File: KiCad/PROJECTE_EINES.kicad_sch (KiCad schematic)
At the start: 5 parts

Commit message: Errors solucionats
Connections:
- net VBAT_12V renamed +12V
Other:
- sheet ETAPA DE ALIMENTACIO ports: added none; removed VBAT_12V, VDD_3V3
- sheet MICROCONTROLADOR I DEBUG ports: added none; removed VDD_3V3
- sheet SENSORS ports: added none; removed VDD_3V3
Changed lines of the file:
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@@
+	(wire
+		(pts
+			(xy 27.94 44.45) (xy 34.29 44.45)
+		)
+		(stroke
+			(width 0)
+			(type default)
+		)
+	)
 	(wire
 		(pts
@@
 	(wire
 		(pts
-			(xy 172.72 58.42) (xy 171.45 58.42)
+			(xy 22.86 93.98) (xy 27.94 93.98)
 		)
 		(stroke
@@
 		)
 	)
-	(wire
-		(pts
-			(xy 22.86 93.98) (xy 27.94 93.98)
-		)
-		(stroke
-			(width 0)
-			(type default)
-		)
-	)
 	(global_label "WIN_MOTOR_B"
 		(shape output)
@@
 		)
 	)
-	(global_label "VDD_3V3"
-		(shape input)
-		(at 194.31 36.83 180)
-		(effects
-			(font
-				(size 1.27 1.27)
-			)
-			(justify right)
-		)
-		(property "Intersheetrefs" "${INTERSHEET_REFS}"
-			(at 194.31 36.83 0)
-			(effects
-				(font
-					(size 1.27 1.27)
-				)
-				(hide yes)
-			)
-		)
-	)
 	(global_label "DOOR_INA"
 		(shape output)
@@
 		)
 	)
-	(global_label "VBAT_12V"
-		(shape input)
-		(at 27.94 44.45 0)
-		(effects
-			(font
-				(size 1.27 1.27)
-			)
-			(justify left)
-		)
-		(property "Intersheetrefs" "${INTERSHEET_REFS}"
-			(at 27.94 44.45 0)
-			(effects
-				(font
-					(size 1.27 1.27)
-				)
-				(hide yes)
-			)
-		)
-	)
 	(global_label "UART_RX"
 		(shape output)
@@
 		)
 	)
-	(global_label "VDD_3V3"
-		(shape input)
-		(at 40.64 24.13 0)
-		(effects
-			(font
-				(size 1.27 1.27)
-			)
-			(justify left)
-		)
-		(property "Intersheetrefs" "${INTERSHEET_REFS}"
-			(at 40.64 24.13 90)
-			(effects
-				(font
-					(size 1.27 1.27)
-				)
-				(hide yes)
-			)
-		)
-	)
 	(global_label "DOOR_MOTOR_B"
 		(shape output)
@@
 		)
 	)
-	(global_label "VDD_3V3"
-		(shape output)
-		(at 104.14 67.31 0)
-		(effects
-			(font
-				(size 1.27 1.27)
-			)
-			(justify left)
-		)
-		(property "Intersheetrefs" "${INTERSHEET_REFS}"
-			(at 104.14 67.31 0)
-			(effects
-				(font
-					(size 1.27 1.27)
-				)
-				(hide yes)
-			)
-		)
-	)
 	(global_label "WIN_DIAGA"
 		(shape output)
@@
 		)
 	)
-	(global_label "VDD_3V3"
-		(shape input)
-		(at 118.11 83.82 90)
-		(effects
-			(font
-				(size 1.27 1.27)
-			)
-			(justify left)
-		)
-		(property "Intersheetrefs" "${INTERSHEET_REFS}"
-			(at 118.11 83.82 0)
-			(effects
-				(font
-					(size 1.27 1.27)
-				)
-				(hide yes)
-			)
-		)
-	)
 	(global_label "DOOR_PWM"
 		(shape output)
@@
 		)
 	)
-	(global_label "VBAT_12V"
-		(shape input)
-		(at 60.96 49.53 180)
-		(effects
-			(font
-				(size 1.27 1.27)
-			)
-			(justify right)
-		)
-		(property "Intersheetrefs" "${INTERSHEET_REFS}"
-			(at 60.96 49.53 0)
-			(effects
-				(font
-					(size 1.27 1.27)
-				)
-				(hide yes)
+	(symbol
+		(lib_id "power:+3.3V")
+		(at 40.64 24.13 0)
+		(unit 1)
+		(exclude_from_sim no)
+		(in_bom yes)
+		(on_board yes)
+		(dnp no)
+		(fields_autoplaced yes)
+		(property "Reference" "#PWR03"
+			(at 40.64 27.94 0)
+			(effects
+				(font
+					(size 1.27 1.27)
+				)
+				(hide yes)
+			)
+		)
+		(property "Value" "+3.3V"
+			(at 40.64 19.05 0)
+			(effects
+				(font
+					(size 1.27 1.27)
+				)
+			)
+		)
+		(property "Footprint" ""
+			(at 40.64 24.13 0)
+			(effects
+				(font
+					(size 1.27 1.27)
+				)
+				(hide yes)
+			)
+		)
+		(property "Datasheet" ""
+			(at 40.64 24.13 0)
+			(effects
+				(font
+					(size 1.27 1.27)
+				)
+				(hide yes)
+			)
+		)
+		(property "Description" "Power symbol creates a global label with name \"+3.3V\""
+			(at 40.64 24.13 0)
+			(effects
+				(font
+					(size 1.27 1.27)
+				)
+				(hide yes)
+			)
+		)
+		(pin "1"
+		)
+		(instances
+			(project ""
+				(path "/347831db-5db9-4aff-ad32-e56fd770e219"
+					(reference "#PWR03")
+					(unit 1)
+				)
 			)
 		)
@@
 	)
 	(symbol
-		(lib_id "power:+3.3V")
-		(at 40.64 24.13 0)
-		(unit 1)
-		(exclude_from_sim no)
-		(in_bom yes)
-		(on_board yes)
-		(dnp no)
-		(fields_autoplaced yes)
-		(property "Reference" "#PWR03"
-			(at 40.64 27.94 0)
-			(effects
-				(font
-					(size 1.27 1.27)
-				)
-				(hide yes)
-			)
-		)
-		(property "Value" "+3.3V"
-			(at 40.64 19.05 0)
-			(effects
-				(font
-					(size 1.27 1.27)
-				)
-			)
-		)
-		(property "Footprint" ""
-			(at 40.64 24.13 0)
-			(effects
-				(font
-					(size 1.27 1.27)
-				)
-				(hide yes)
-			)
-		)
-		(property "Datasheet" ""
-			(at 40.64 24.13 0)
-			(effects
-				(font
-					(size 1.27 1.27)
-				)
-				(hide yes)
-			)
-		)
-		(property "Description" "Power symbol creates a global label with name \"+3.3V\""
-			(at 40.64 24.13 0)
-			(effects
-				(font
-					(size 1.27 1.27)
-				)
-				(hide yes)
-			)
-		)
-		(pin "1"
-		)
-		(instances
-			(project ""
-				(path "/347831db-5db9-4aff-ad32-e56fd770e219"
-					(reference "#PWR03")
-					(unit 1)
-				)
-			)
-		)
-	)
-	(symbol
 		(lib_id "Connector:Conn_01x02_Pin")
 		(at 21.59 77.47 0)
@@
 				(path "/347831db-5db9-4aff-ad32-e56fd770e219"
 					(reference "J_MOTOR_DOOR1")
+					(unit 1)
+				)
+			)
+		)
+	)
+	(symbol
+		(lib_id "power:+12V")
+		(at 34.29 44.45 0)
+		(unit 1)
+		(exclude_from_sim no)
+		(in_bom yes)
+		(on_board yes)
+		(dnp no)
+		(fields_autoplaced yes)
+		(property "Reference" "#PWR051"
+			(at 34.29 48.26 0)
+			(effects
+				(font
+					(size 1.27 1.27)
+				)
+				(hide yes)
+			)
+		)
+		(property "Value" "+12V"
+			(at 34.29 39.37 0)
+			(effects
+				(font
+					(size 1.27 1.27)
+				)
+			)
+		)
+		(property "Footprint" ""
+			(at 34.29 44.45 0)
+			(effects
+				(font
+					(size 1.27 1.27)
+				)
+				(hide yes)
+			)
+		)
+		(property "Datasheet" ""
+			(at 34.29 44.45 0)
+			(effects
+				(font
+					(size 1.27 1.27)
+				)
+				(hide yes)
+			)
+		)
+		(property "Description" "Power symbol creates a global label with name \"+12V\""
+			(at 34.29 44.45 0)
+			(effects
+				(font
+					(size 1.27 1.27)
+				)
+				(hide yes)
+			)
+		)
+		(pin "1"
+		)
+		(instances
+			(project "PROJECTE_EINES"
+				(path "/347831db-5db9-4aff-ad32-e56fd770e219"
+					(reference "#PWR051")
 					(unit 1)
 				)
@@
 		(on_board yes)
 		(dnp no)
-		(property "Reference" "#FLG04"
+		(property "Reference" "#FLG01"
 			(at 22.86 92.075 0)
 			(effects
@@
 			(project "PROJECTE_EINES"
 				(path "/347831db-5db9-4aff-ad32-e56fd770e219"
-					(reference "#FLG04")
+					(reference "#FLG01")
 					(unit 1)
 				)
@@
 			)
 		)
-		(pin "VDD_3V3" input
-			(at 194.31 36.83 180)
-			(effects
-				(font
-					(size 1.27 1.27)
-				)
-				(justify left)
-			)
-		)
 		(pin "WIN_LIMIT" output
 			(at 194.31 44.45 180)
@@
 			)
 		)
-		(pin "VDD_3V3" input
-			(at 118.11 83.82 90)
-			(effects
-				(font
-					(size 1.27 1.27)
-				)
-				(justify right)
-			)
-		)
 		(pin "WIN_BTN_DOWN" input
 			(at 153.67 88.9 0)
@@
 			)
 		)
-		(pin "VBAT_12V" input
-			(at 60.96 49.53 180)
-			(effects
-				(font
-					(size 1.27 1.27)
-				)
-				(justify left)
-			)
-		)
 		(pin "VBAT_PROT" output
 			(at 104.14 64.77 0)
 			(effects
 				(font
-					(size 1.27 1.27)
-				)
-				(justify right)
-			)
-		)
-		(pin "VDD_3V3" output
-			(at 104.14 67.31 0)
-			(effects
-				(font

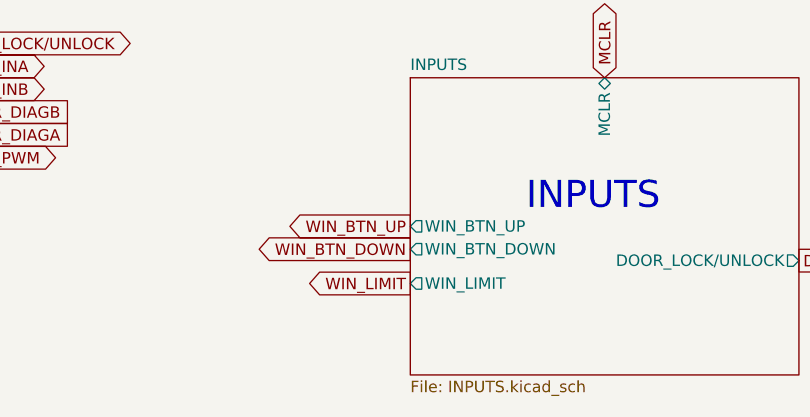
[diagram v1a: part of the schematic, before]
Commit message: REORDENACIÓ DEL MICRO
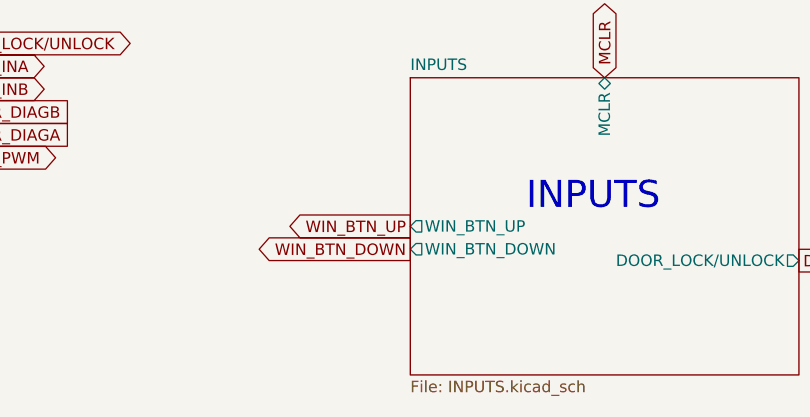
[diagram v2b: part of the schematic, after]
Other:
- sheet INPUTS ports: added none; removed WIN_LIMIT
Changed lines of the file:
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@@
-		)
-	)
-	(global_label "WIN_LIMIT"
-		(shape output)
-		(at 205.74 148.59 180)
-		(effects
-			(font
-				(size 1.27 1.27)
-			)
-			(justify right)
-		)
-		(property "Intersheetrefs" "${INTERSHEET_REFS}"
-			(at 205.74 148.59 0)
-			(effects
-				(font
-					(size 1.27 1.27)
-				)
-				(hide yes)
-			)
 		)
 	)
@@
 			(effects
 				(font
-					(size 1.27 1.27)
-				)
-				(justify left)
-			)
-		)
-		(pin "WIN_LIMIT" output
-			(at 205.74 148.59 180)
-			(effects
-				(font

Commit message: V1 Routing
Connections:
- net GND: now also J_DEBUG1.1 (Pin_1); no longer J_DEBUG1.3 (Pin_3)
- net MCLR: now also J_DEBUG1.3 (Pin_3); no longer J_DEBUG1.1 (Pin_1)
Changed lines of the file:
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@@
+	)
+	(junction
+		(at 30.48 21.59)
+		(diameter 0)
+		(color 0 0 0 0)
 	)
 	(junction
@@
 	(wire
 		(pts
-			(xy 26.67 24.13) (xy 40.64 24.13)
+			(xy 26.67 24.13) (xy 45.72 24.13)
 		)
 		(stroke
@@
 	(wire
 		(pts
-			(xy 40.64 26.67) (xy 40.64 27.94)
+			(xy 20.32 93.98) (xy 22.86 93.98)
 		)
 		(stroke
@@
 	(wire
 		(pts
-			(xy 20.32 93.98) (xy 22.86 93.98)
+			(xy 20.32 95.25) (xy 20.32 93.98)
 		)
 		(stroke
@@
 	(wire
 		(pts
-			(xy 20.32 95.25) (xy 20.32 93.98)
+			(xy 26.67 21.59) (xy 30.48 21.59)
 		)
 		(stroke
@@
 	(wire
 		(pts
-			(xy 26.67 26.67) (xy 40.64 26.67)
+			(xy 43.18 95.25) (xy 43.18 93.98)
 		)
 		(stroke
@@
 	(wire
 		(pts
-			(xy 43.18 95.25) (xy 43.18 93.98)
+			(xy 30.48 46.99) (xy 30.48 49.53)
 		)
 		(stroke
@@
 	(wire
 		(pts
-			(xy 30.48 46.99) (xy 30.48 49.53)
+			(xy 22.86 93.98) (xy 27.94 93.98)
 		)
 		(stroke
@@
 		)
 	)
-	(wire
-		(pts
-			(xy 22.86 93.98) (xy 27.94 93.98)
-		)
-		(stroke
-			(width 0)
-			(type default)
-		)
-	)
 	(global_label "WIN_MOTOR_B"
 		(shape output)
@@
 	(global_label "MCLR"
 		(shape input)
-		(at 26.67 21.59 0)
-		(effects
-			(font
-				(size 1.27 1.27)
-			)
-			(justify left)
-		)
-		(property "Intersheetrefs" "${INTERSHEET_REFS}"
-			(at 26.67 21.59 0)
+		(at 26.67 26.67 0)
+		(effects
+			(font
+				(size 1.27 1.27)
+			)
+			(justify left)
+		)
+		(property "Intersheetrefs" "${INTERSHEET_REFS}"
+			(at 26.67 26.67 0)
 			(effects
 				(font
@@
 	(symbol
 		(lib_id "power:+3.3V")
-		(at 40.64 24.13 0)
+		(at 45.72 24.13 0)
 		(unit 1)
 		(exclude_from_sim no)
@@
 		(dnp no)
 		(fields_autoplaced yes)
-		(property "Reference" "#PWR03"
-			(at 40.64 27.94 0)
+		(property "Reference" "#PWR04"
+			(at 45.72 27.94 0)
 			(effects
 				(font
@@
 		)
 		(property "Value" "+3.3V"
-			(at 40.64 19.05 0)
+			(at 45.72 19.05 0)
 			(effects
 				(font
@@
 		)
 		(property "Footprint" ""
-			(at 40.64 24.13 0)
+			(at 45.72 24.13 0)
 			(effects
 				(font
@@
 		)
 		(property "Datasheet" ""
-			(at 40.64 24.13 0)
+			(at 45.72 24.13 0)
 			(effects
 				(font
@@
 		)
 		(property "Description" "Power symbol creates a global label with name \"+3.3V\""
-			(at 40.64 24.13 0)
+			(at 45.72 24.13 0)
 			(effects
 				(font
@@
 			(project ""
 				(path "/347831db-5db9-4aff-ad32-e56fd770e219"
-					(reference "#PWR03")
+					(reference "#PWR04")
 					(unit 1)
 				)
@@
 		(dnp no)
 		(fields_autoplaced yes)
-		(property "Reference" "#PWR05"
+		(property "Reference" "#PWR06"
 			(at 43.18 101.6 0)
 			(effects
@@
 			(project ""
 				(path "/347831db-5db9-4aff-ad32-e56fd770e219"
-					(reference "#PWR05")
+					(reference "#PWR06")
 					(unit 1)
 				)
@@
 	)
 	(symbol
+		(lib_id "power:PWR_FLAG")
+		(at 30.48 21.59 270)
+		(unit 1)
+		(exclude_from_sim no)
+		(in_bom yes)
+		(on_board yes)
+		(dnp no)
+		(fields_autoplaced yes)
+		(property "Reference" "#FLG07"
+			(at 32.385 21.59 0)
+			(effects
+				(font
+					(size 1.27 1.27)
+				)
+				(hide yes)
+			)
+		)
+		(property "Value" "PWR_FLAG"
+			(at 34.29 21.5899 90)
+			(effects
+				(font
+					(size 1.27 1.27)
+				)
+				(justify left)
+			)
+		)
+		(property "Footprint" ""
+			(at 30.48 21.59 0)
+			(effects
+				(font
+					(size 1.27 1.27)
+				)
+				(hide yes)
+			)
+		)
+		(property "Datasheet" "~"
+			(at 30.48 21.59 0)
+			(effects
+				(font
+					(size 1.27 1.27)
+				)
+				(hide yes)
+			)
+		)
+		(property "Description" "Special symbol for telling ERC where power comes from"
+			(at 30.48 21.59 0)
+			(effects
+				(font
+					(size 1.27 1.27)
+				)
+				(hide yes)
+			)
+		)
+		(pin "1"
+		)
+		(instances
+			(project ""
+				(path "/347831db-5db9-4aff-ad32-e56fd770e219"
+					(reference "#FLG07")
+					(unit 1)
+				)
+			)
+		)
+	)
+	(symbol
 		(lib_id "Connector:Conn_01x02_Pin")
 		(at 22.86 44.45 0)
@@
 		(dnp no)
 		(fields_autoplaced yes)
-		(property "Reference" "#PWR051"
+		(property "Reference" "#PWR03"
 			(at 34.29 48.26 0)
 			(effects
@@
 			(project "PROJECTE_EINES"
 				(path "/347831db-5db9-4aff-ad32-e56fd770e219"
-					(reference "#PWR051")
+					(reference "#PWR03")
 					(unit 1)
 				)
@@
 	(symbol
 		(lib_id "power:GND")
-		(at 40.64 27.94 0)
+		(at 30.48 21.59 0)
 		(unit 1)
 		(exclude_from_sim no)
@@
 		(dnp no)
 		(fields_autoplaced yes)
-		(property "Reference" "#PWR04"
-			(at 40.64 34.29 0)
+		(property "Reference" "#PWR05"
+			(at 30.48 27.94 0)
 			(effects
 				(font
@@
 		)
 		(property "Value" "GND"
-			(at 40.64 33.02 0)
-			(effects
-				(font
-					(size 1.27 1.27)
-				)
+			(at 30.48 26.67 0)
+			(effects
+				(font
+					(size 1.27 1.27)
+				)
+				(hide yes)
 			)
 		)
 		(property "Footprint" ""
-			(at 40.64 27.94 0)
+			(at 30.48 21.59 0)
 			(effects
 				(font
@@
 		)
 		(property "Datasheet" ""
-			(at 40.64 27.94 0)
+			(at 30.48 21.59 0)
 			(effects
 				(font
@@
 		)
 		(property "Description" "Power symbol creates a global label with name \"GND\" , ground"
-			(at 40.64 27.94 0)
+			(at 30.48 21.59 0)
 			(effects
 				(font
@@
 			(project "PROJECTE_EINES"
 				(path "/347831db-5db9-4aff-ad32-e56fd770e219"
-					(reference "#PWR04")
+					(reference "#PWR05")
 					(unit 1)
 				)

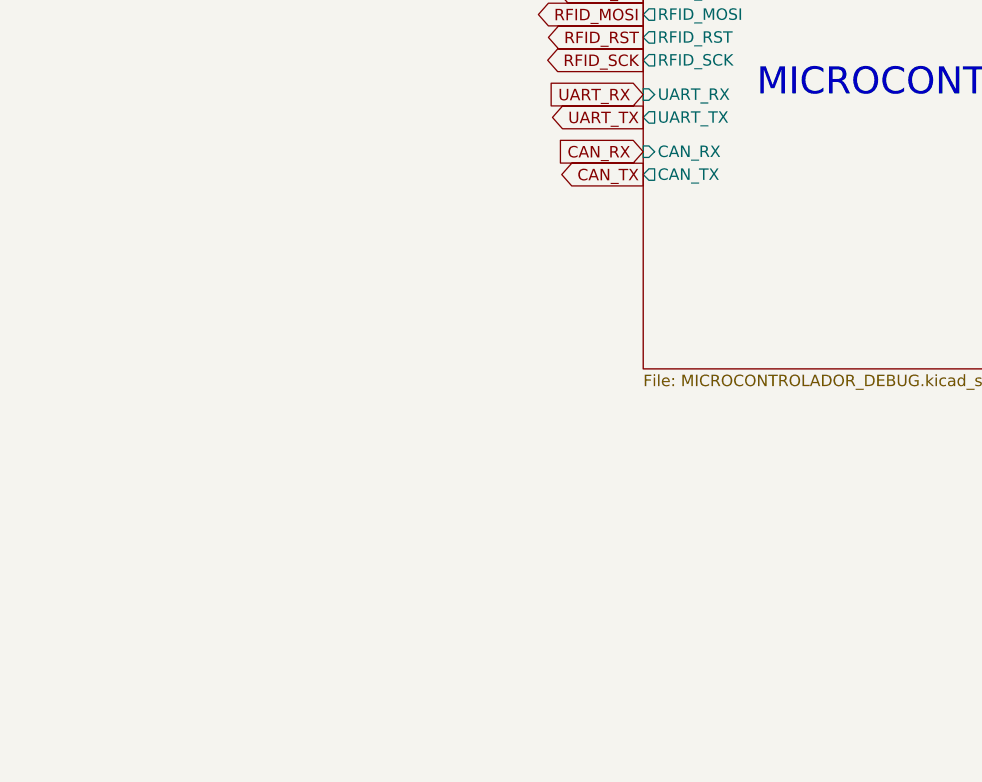
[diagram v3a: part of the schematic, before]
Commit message: Update dels testpins
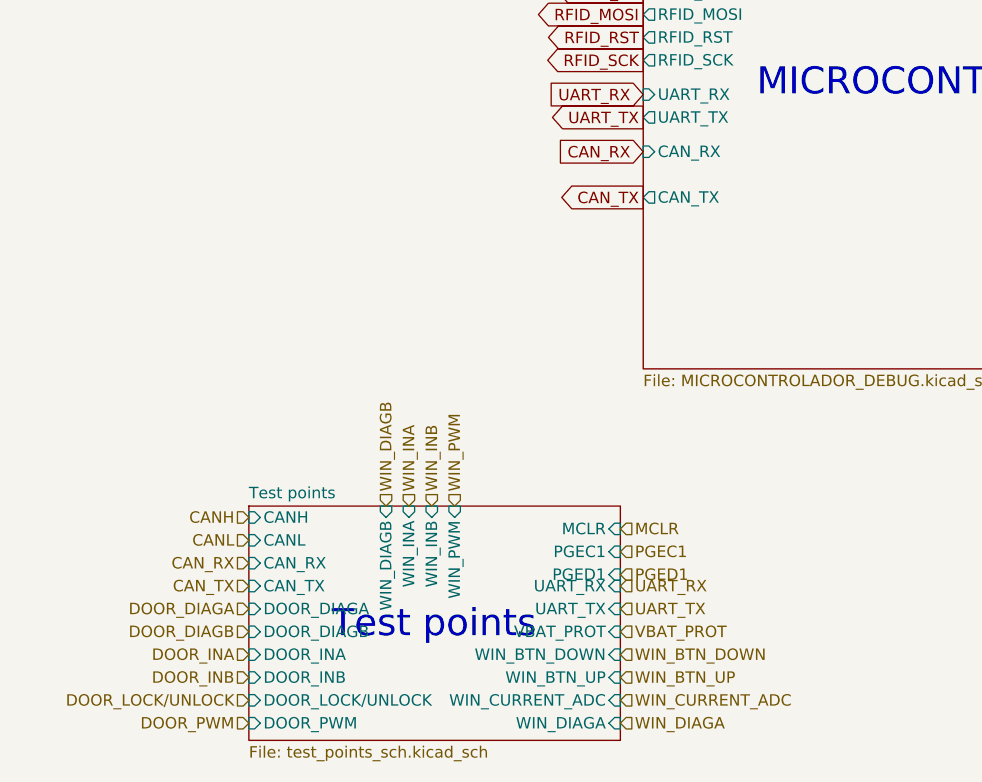
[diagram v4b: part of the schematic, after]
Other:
- added sheet Test points (test_points_sch.kicad_sch)
- note added: "Test points"

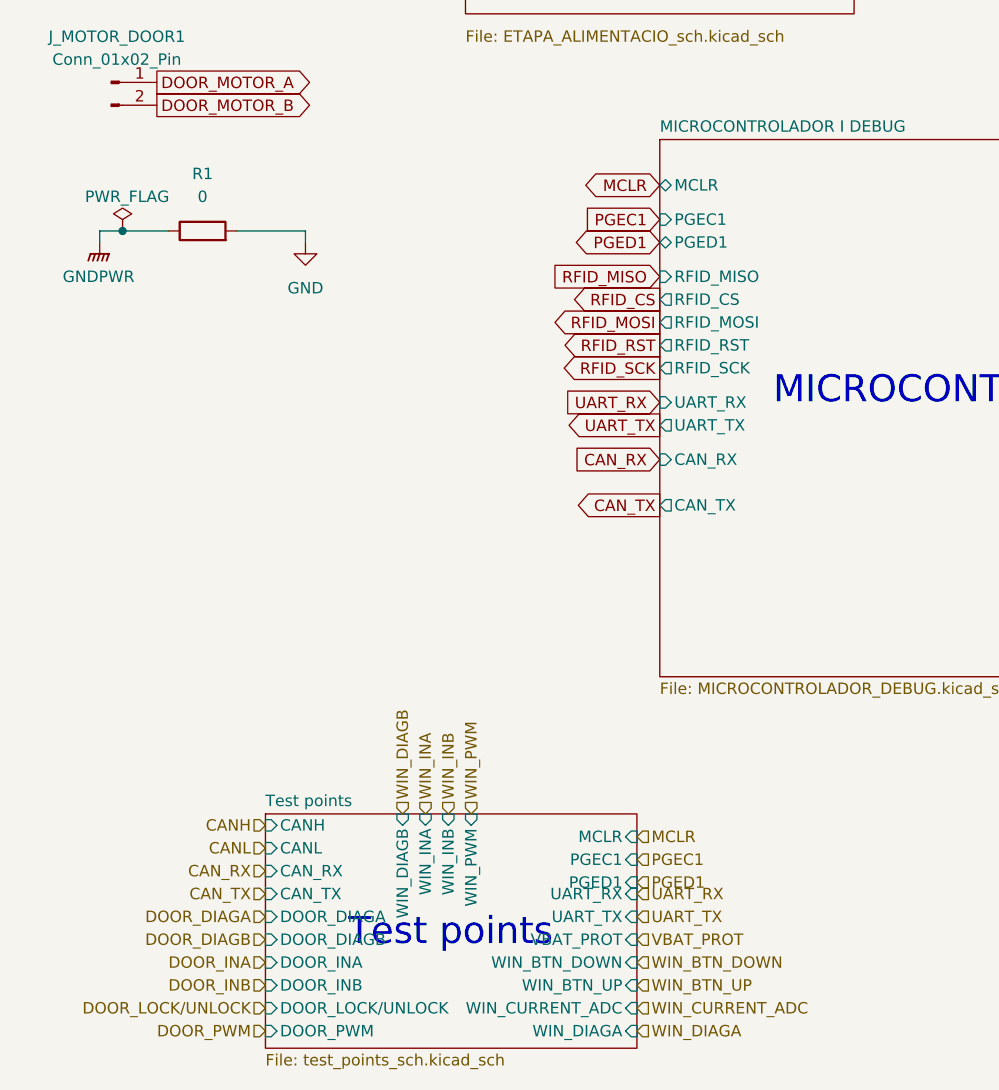
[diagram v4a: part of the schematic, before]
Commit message: Actualització dels test points
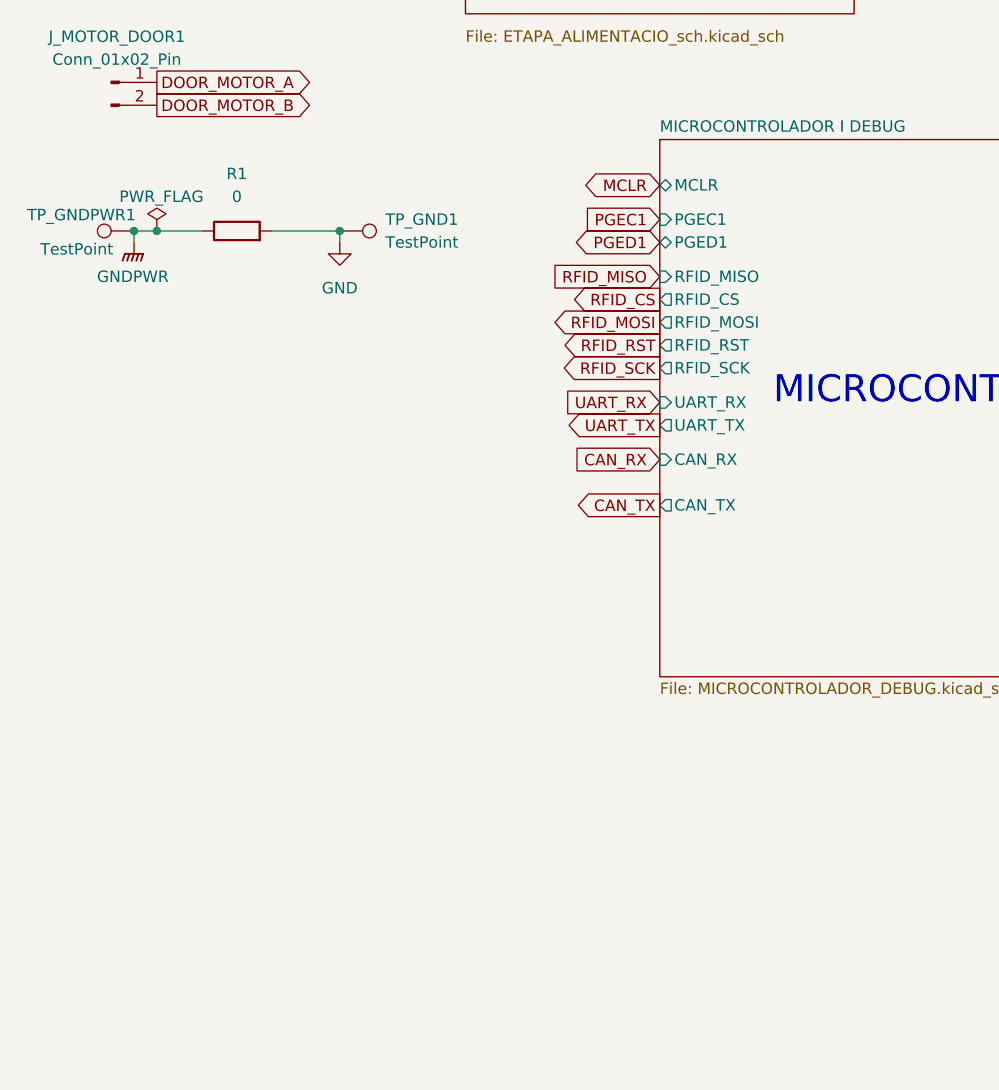
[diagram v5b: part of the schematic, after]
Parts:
- added TP_GND1, TP_GNDPWR1: TestPoint, TestPoint:TestPoint_Pad_D1.5mm, symbol Connector:TestPoint
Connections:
- net GND: now also TP_GND1.1
- net GNDPWR: now also TP_GNDPWR1.1
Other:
- removed sheet Test points
- note removed: "Test points"
- moved on the sheet: R1

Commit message: Versio final KiCad, BOM i Diagrama de Blocs
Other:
- note added: "Conector DEBUG"
- note added: "Conector entrada +12V"
- note added: "Conector motor finestra"
- note added: "Conector motor porta"
- note added: "Unió de masses"
- moved on the sheet: J_DEBUG1, J_MOTOR_DOOR1, J_MOTOR_WIN1, J_PWR1, R1, TP_GND1, TP_GNDPWR1
